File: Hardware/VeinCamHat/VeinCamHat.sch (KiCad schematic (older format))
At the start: 67 parts

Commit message: Hardware Updates
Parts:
- removed BT?: 3v7 LiPo, symbol badgeLibrary:Battery_Cell
- removed D? (x6): SFH7252, symbol VeinCam:SFH7252
- removed Q? (x2): BSD235N, symbol VeinCam:BSD235N
- removed U?: MCP73871, symbol VeinCam:MCP73871
- removed U?: MCP3021, symbol VeinCam:MCP3021
- removed V?: VLIPO, symbol VeinCam:VLIPO
- added BT?: 3v7 LIPO, symbol Device:Battery_Cell
- added D? (x6): SFH7252, symbol VeinCam_Symbols:SFH7252
- added Q? (x2): BSD235N, symbol VeinCam_Symbols:BSD235N
- added U?: MCP3021, symbol VeinCam_Symbols:MCP3021
- added U?: MCP73871, symbol VeinCam_Symbols:MCP73871
- added V?: VLIPO, symbol VeinCam_Symbols:VLIPO
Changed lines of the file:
@@
 Comment4 ""
 $EndDescr
-$Comp
-L VeinCam:SFH7252 D?
-U 1 1 5C87F7A5
-P 1700 5800
-F 0 "D?" H 1700 6050 50  0000 C CNN
-F 1 "SFH7252" H 1700 5550 50  0000 C CNN
-F 2 "" H 1730 5800 50  0001 C CNN
-F 3 "~" H 1730 5800 50  0001 C CNN
-	1    1700 5800
-	1    0    0    -1
-$EndComp
-$Comp
-L VeinCam:SFH7252 D?
-U 1 1 5C87F803
-P 1700 6450
-F 0 "D?" H 1700 6700 50  0000 C CNN
-F 1 "SFH7252" H 1700 6200 50  0000 C CNN
-F 2 "" H 1730 6450 50  0001 C CNN
-F 3 "~" H 1730 6450 50  0001 C CNN
-	1    1700 6450
-	1    0    0    -1
-$EndComp
-$Comp
-L VeinCam:SFH7252 D?
-U 1 1 5C87F83D
-P 2650 6450
-F 0 "D?" H 2650 6700 50  0000 C CNN
-F 1 "SFH7252" H 2650 6200 50  0000 C CNN
-F 2 "" H 2680 6450 50  0001 C CNN
-F 3 "~" H 2680 6450 50  0001 C CNN
-	1    2650 6450
-	1    0    0    -1
-$EndComp
-$Comp
-L VeinCam:SFH7252 D?
-U 1 1 5C87F881
-P 2650 5800
-F 0 "D?" H 2650 6050 50  0000 C CNN
-F 1 "SFH7252" H 2650 5550 50  0000 C CNN
-F 2 "" H 2680 5800 50  0001 C CNN
-F 3 "~" H 2680 5800 50  0001 C CNN
-	1    2650 5800
-	1    0    0    -1
-$EndComp
-$Comp
-L VeinCam:SFH7252 D?
-U 1 1 5C87F8BF
-P 3600 5800
-F 0 "D?" H 3600 6050 50  0000 C CNN
-F 1 "SFH7252" H 3600 5550 50  0000 C CNN
-F 2 "" H 3630 5800 50  0001 C CNN
-F 3 "~" H 3630 5800 50  0001 C CNN
-	1    3600 5800
-	1    0    0    -1
-$EndComp
-$Comp
-L VeinCam:SFH7252 D?
-U 1 1 5C87F8FB
-P 3600 6450
-F 0 "D?" H 3600 6700 50  0000 C CNN
-F 1 "SFH7252" H 3600 6200 50  0000 C CNN
-F 2 "" H 3630 6450 50  0001 C CNN
-F 3 "~" H 3630 6450 50  0001 C CNN
-	1    3600 6450
-	1    0    0    -1
-$EndComp
 Text Notes 4550 650  0    100  ~ 0
 RPi Connector
@@
 Text Notes 6250 6800 0    100  ~ 0
 M2.5
-$Comp
-L VeinCam:BSD235N Q?
-U 1 1 5C875BEA
-P 4000 6950
-F 0 "Q?" H 4206 6996 50  0000 L CNN
-F 1 "BSD235N" H 4206 6905 50  0000 L CNN
-F 2 "" H 4200 6950 50  0001 C CNN
-F 3 "~" H 4200 6950 50  0001 C CNN
-	1    4000 6950
-	1    0    0    -1
-$EndComp
-$Comp
-L VeinCam:BSD235N Q?
-U 2 1 5C875C59
-P 5450 6950
-F 0 "Q?" H 5656 6996 50  0000 L CNN
-F 1 "BSD235N" H 5656 6905 50  0000 L CNN
-F 2 "" H 5650 6950 50  0001 C CNN
-F 3 "~" H 5650 6950 50  0001 C CNN
-	2    5450 6950
-	1    0    0    -1
-$EndComp
 Wire Wire Line
 	2000 5700 2350 5700
@@
 Text Notes 1350 3100 0    100  ~ 0
 Charge Only USB\n
-$Comp
-L VeinCam:MCP73871 U?
-U 1 1 5C935F2C
-P 9200 2450
-F 0 "U?" H 8850 3350 50  0000 C CNN
-F 1 "MCP73871" H 8950 3250 39  0000 C CNN
-F 2 "" H 9100 3000 100 0001 C CNN
-F 3 "" H 9100 3000 100 0001 C CNN
-	1    9200 2450
-	1    0    0    -1
-$EndComp
 Wire Wire Line
 	8700 1900 8550 1900
@@
 Connection ~ 9800 2050
 $Comp
-L VeinCam:VLIPO V?
-U 1 1 5CA63BBA
-P 10500 1800
-F 0 "V?" H 10500 1800 50  0001 C CNN
-F 1 "VLIPO" H 10400 1900 50  0000 L CNN
-F 2 "" H 10500 1800 50  0001 C CNN
-F 3 "" H 10500 1800 50  0001 C CNN
-	1    10500 1800
-	1    0    0    -1
-$EndComp
-$Comp
 L Device:C C?
 U 1 1 5CA6A895
@@
 F 3 "" H 10350 3000 50  0001 C CNN
 	1    10350 3000
-	1    0    0    -1
-$EndComp
-$Comp
-L badgeLibrary:Battery_Cell BT?
-U 1 1 5CAEAF18
-P 10700 2700
-F 0 "BT?" H 10818 2746 50  0000 L CNN
-F 1 "3v7 LiPo" H 10818 2655 50  0000 L CNN
-F 2 "" H 10700 2700 50  0001 C CNN
-F 3 "" H 10700 2700 50  0001 C CNN
-	1    10700 2700
 	1    0    0    -1
 $EndComp
@@
 SDA
 $Comp
-L VeinCam:MCP3021 U?
-U 1 1 5D86629E
+L VeinCam_Symbols:BSD235N Q?
+U 1 1 5C89B330
+P 4000 6950
+F 0 "Q?" H 4206 6996 50  0000 L CNN
+F 1 "BSD235N" H 4206 6905 50  0000 L CNN
+F 2 "" H 4200 6950 50  0001 C CNN
+F 3 "~" H 4200 6950 50  0001 C CNN
+	1    4000 6950
+	1    0    0    -1
+$EndComp
+$Comp
+L VeinCam_Symbols:BSD235N Q?
+U 2 1 5C89B4BB
+P 5450 6950
+F 0 "Q?" H 5656 6996 50  0000 L CNN
+F 1 "BSD235N" H 5656 6905 50  0000 L CNN
+F 2 "" H 5650 6950 50  0001 C CNN
+F 3 "~" H 5650 6950 50  0001 C CNN
+	2    5450 6950
+	1    0    0    -1
+$EndComp
+$Comp
+L VeinCam_Symbols:MCP3021 U?
+U 1 1 5C89B58C
 P 2200 1950
 F 0 "U?" H 2200 2125 50  0000 C CNN
 F 1 "MCP3021" H 2200 2034 50  0000 C CNN
 F 2 "" H 2200 1950 100 0001 C CNN
-F 3 "" H 2200 1950 100 0001 C CNN
+F 3 "~" H 2200 1950 100 0001 C CNN
 	1    2200 1950
 	1    0    0    -1
 $EndComp
+$Comp
+L VeinCam_Symbols:MCP73871 U?
+U 1 1 5C89BAE3
+P 9200 2450
+F 0 "U?" H 8850 3350 50  0000 C CNN
+F 1 "MCP73871" H 9000 3250 50  0000 C CNN
+F 2 "" H 9100 3000 100 0001 C CNN
+F 3 "~" H 9100 3000 100 0001 C CNN
+	1    9200 2450
+	1    0    0    -1
+$EndComp
+$Comp
+L VeinCam_Symbols:SFH7252 D?
+U 1 1 5C89C23B
+P 1700 5800
+F 0 "D?" H 1700 6050 50  0000 C CNN
+F 1 "SFH7252" H 1700 5550 50  0000 C CNN
+F 2 "" H 1730 5800 50  0001 C CNN
+F 3 "~" H 1730 5800 50  0001 C CNN
+	1    1700 5800
+	1    0    0    -1
+$EndComp
+$Comp
+L VeinCam_Symbols:SFH7252 D?
+U 1 1 5C89C451
+P 1700 6450
+F 0 "D?" H 1700 6700 50  0000 C CNN
+F 1 "SFH7252" H 1700 6200 50  0000 C CNN
+F 2 "" H 1730 6450 50  0001 C CNN
+F 3 "~" H 1730 6450 50  0001 C CNN
+	1    1700 6450
+	1    0    0    -1
+$EndComp
+$Comp
+L VeinCam_Symbols:SFH7252 D?
+U 1 1 5C89C4E7
+P 2650 6450
+F 0 "D?" H 2650 6700 50  0000 C CNN
+F 1 "SFH7252" H 2650 6200 50  0000 C CNN
+F 2 "" H 2680 6450 50  0001 C CNN
+F 3 "~" H 2680 6450 50  0001 C CNN
+	1    2650 6450
+	1    0    0    -1
+$EndComp
+$Comp
+L VeinCam_Symbols:SFH7252 D?
+U 1 1 5C89C583
+P 3600 6450
+F 0 "D?" H 3600 6700 50  0000 C CNN
+F 1 "SFH7252" H 3600 6200 50  0000 C CNN
+F 2 "" H 3630 6450 50  0001 C CNN
+F 3 "~" H 3630 6450 50  0001 C CNN
+	1    3600 6450
+	1    0    0    -1
+$EndComp
+$Comp
+L VeinCam_Symbols:SFH7252 D?
+U 1 1 5C89C61B
+P 3600 5800
+F 0 "D?" H 3600 6050 50  0000 C CNN
+F 1 "SFH7252" H 3600 5550 50  0000 C CNN
+F 2 "" H 3630 5800 50  0001 C CNN
+F 3 "~" H 3630 5800 50  0001 C CNN
+	1    3600 5800
+	1    0    0    -1
+$EndComp
+$Comp
+L VeinCam_Symbols:SFH7252 D?
+U 1 1 5C89C6B9
+P 2650 5800
+F 0 "D?" H 2650 6050 50  0000 C CNN
+F 1 "SFH7252" H 2650 5550 50  0000 C CNN
+F 2 "" H 2680 5800 50  0001 C CNN
+F 3 "~" H 2680 5800 50  0001 C CNN
+	1    2650 5800
+	1    0    0    -1
+$EndComp
+$Comp
+L VeinCam_Symbols:VLIPO V?
+U 1 1 5C89C9D5
+P 10500 1800
+F 0 "V?" H 10500 1800 50  0001 C CNN
+F 1 "VLIPO" H 10400 1900 50  0000 L CNN
+F 2 "" H 10500 1800 50  0001 C CNN
+F 3 "~" H 10500 1800 50  0001 C CNN
+	1    10500 1800
+	1    0    0    -1
+$EndComp
+$Comp
+L Device:Battery_Cell BT?
+U 1 1 5C89CDF3
+P 10700 2750
+F 0 "BT?" H 10818 2846 50  0000 L CNN
+F 1 "3v7 LIPO" H 10818 2755 50  0000 L CNN
+F 2 "" V 10700 2810 50  0001 C CNN
+F 3 "~" V 10700 2810 50  0001 C CNN
+	1    10700 2750
+	1    0    0    -1
+$EndComp

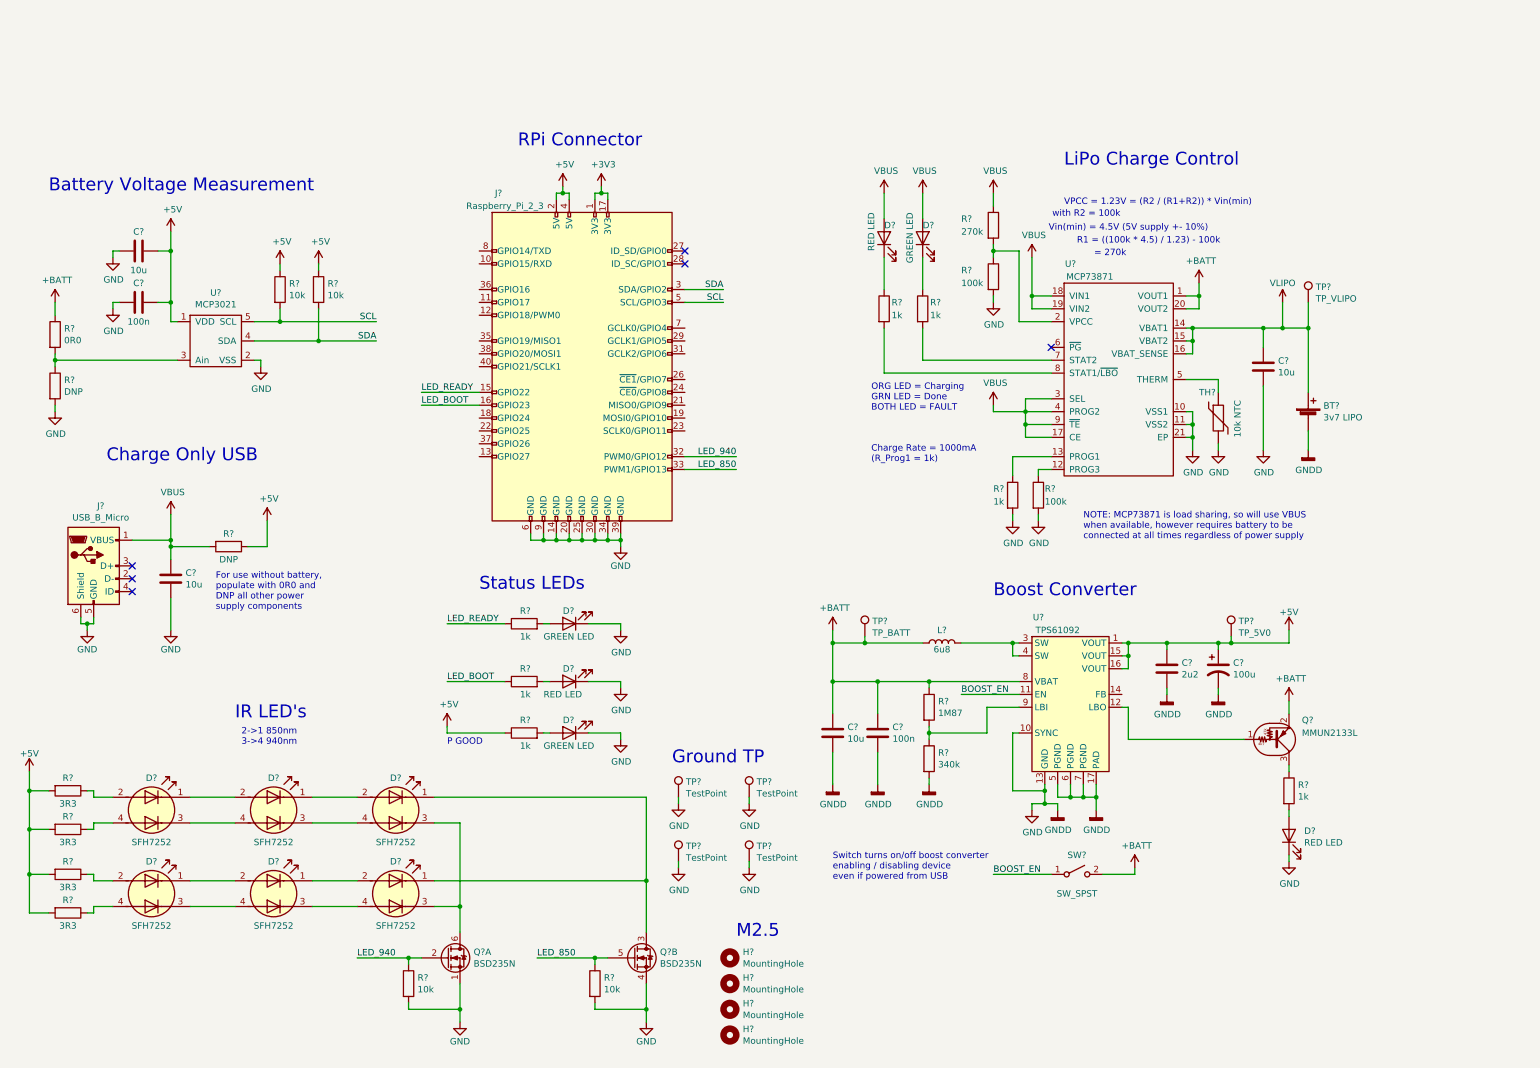
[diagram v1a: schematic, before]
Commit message: Schematic for RPiZero hat completed, BOM generation and Estimated Financials completed.
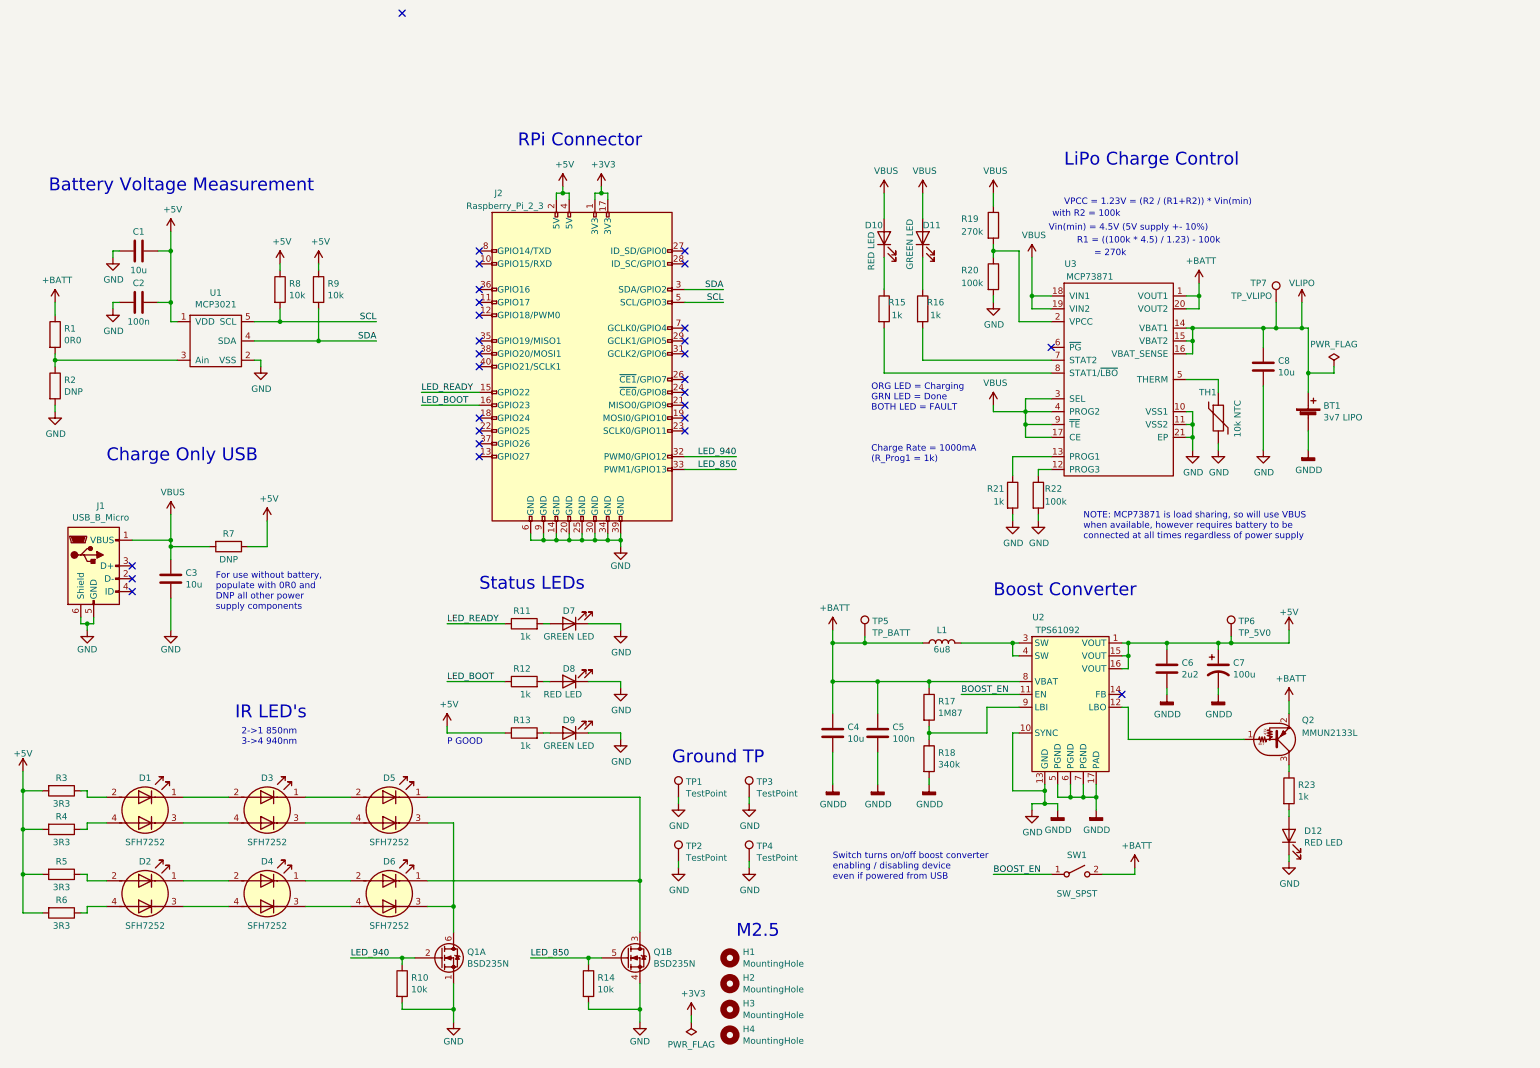
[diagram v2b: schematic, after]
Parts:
- removed V?: VLIPO, symbol VeinCam_Symbols:VLIPO
- BT1: renamed from BT?; footprint (none) -> Connector_JST:JST_XH_S02B-XH-A_1x02_P2.50mm_Horizontal
- C1, C2, C3, C4, C5, C6, C8: renamed from C?; footprint (none) -> Capacitor_SMD:C_0603_1608Metric
- C7: renamed from C?; footprint (none) -> Capacitor_Tantalum_SMD:CP_EIA-7343-31_Kemet-D
- D10, D11, D12, D7, D8, D9: renamed from D?; footprint (none) -> LED_SMD:LED_0805_2012Metric
- H1, H2, H3, H4: renamed from H?; footprint (none) -> MountingHole:MountingHole_2.7mm_M2.5
- Q1: renamed from Q?; footprint (none) -> Package_TO_SOT_SMD:SOT-363_SC-70-6
- Q2: renamed from Q?; footprint (none) -> Package_TO_SOT_SMD:SOT-23
- R1, R10, R11, R12, R13, R14, R15, R16, R17, R18, R19, R2, R20, R21, R22, R23, R3, R4, R5, R6, R8, R9: renamed from R?; footprint (none) -> Resistor_SMD:R_0603_1608Metric
- R7: renamed from R?; footprint (none) -> Resistor_SMD:R_1206_3216Metric
- TH1: renamed from TH?; footprint (none) -> Resistor_SMD:R_0603_1608Metric
- TP1, TP2, TP3, TP4: renamed from TP?; footprint (none) -> TestPoint:TestPoint_THTPad_D1.0mm_Drill0.5mm
- TP5, TP6, TP7: renamed from TP?; footprint (none) -> TestPoint:TestPoint_Pad_D1.0mm
- U1: renamed from U?; footprint (none) -> Package_TO_SOT_SMD:SOT-23-5
- U3: renamed from U?; footprint (none) -> Package_DFN_QFN:QFN-20-1EP_4x4mm_P0.5mm_EP2.5x2.5mm
- gave numbers to parts that had none: 11
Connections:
- no-connect marks 6 -> 28
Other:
- moved on the sheet: D1, D2, D3, D4, D5, D6, Q1A, Q1B, R10, R14, R3, R4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
